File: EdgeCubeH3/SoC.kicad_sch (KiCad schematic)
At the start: 38 parts, among them Q4 NPN, SW1 RST, U1 H3, Y1 24M, Y2 32K

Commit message: Schematic update, PCB started
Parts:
- added R42: 10M, Resistor_SMD:R_0603_1608Metric, symbol Device:R
- added SW2: PWR, Button_Switch_SMD:Button_6x3mm, symbol Switch:SW_Push
- SW1: footprint (none) -> Button_Switch_SMD:Button_6x3mm
- U1: footprint Lib:BGA347_H3_AWT-M -> cm0:FBGA-347_14x14mm_Layout21x21_P0.65mm
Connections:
- net GND: now also SW2.1
- net at R41.1, TP2.1, U1.R1 (PL3): now also SW2.2
- net at C26.2, U1.U4 (X32KOUT), Y2.3: now also R42.1
- net at C27.2, U1.V5 (X32KIN), Y2.1: now also R42.2
- net SPI0_CS: now reaches U1.B15 (PC3)
- net SPI0_CLK: now reaches U1.B16 (PC2)
- net SPI0_MOSI: now reaches U1.C15 (PC0)
- net SPI0_MISO: now reaches U1.C16 (PC1)
- no-connect marks 117 -> 113
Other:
- moved on the sheet: R33

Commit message: PCB design at ~90%
- re-arrangement of components
- connecting dram
- connecting ports
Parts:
- R36: footprint Resistor_SMD:R_0603_1608Metric_Pad0.98x0.95mm_HandSolder -> Resistor_SMD:R_0603_1608Metric
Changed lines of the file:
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@@
 			)
 		)
-		(property "Footprint" "Resistor_SMD:R_0603_1608Metric_Pad0.98x0.95mm_HandSolder"
+		(property "Footprint" "Resistor_SMD:R_0603_1608Metric"
 			(at 238.252 114.3 90)
 			(hide yes)

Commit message: PCB at 95%
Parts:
- removed SW1: RST, Button_Switch_SMD:Button_6x3mm, symbol Switch:SW_Push
- removed SW2: PWR, Button_Switch_SMD:Button_6x3mm, symbol Switch:SW_Push

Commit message: Compleating PCB design
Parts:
- added C45: 100n, Resistor_SMD:R_0402_1005Metric, symbol Device:C
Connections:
- net GND: now also C45.2
- net VREF: now also C45.1
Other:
- note added: "RESET Circuit"
- moved on the sheet: C29, C30, Q4, R37, R38, R39

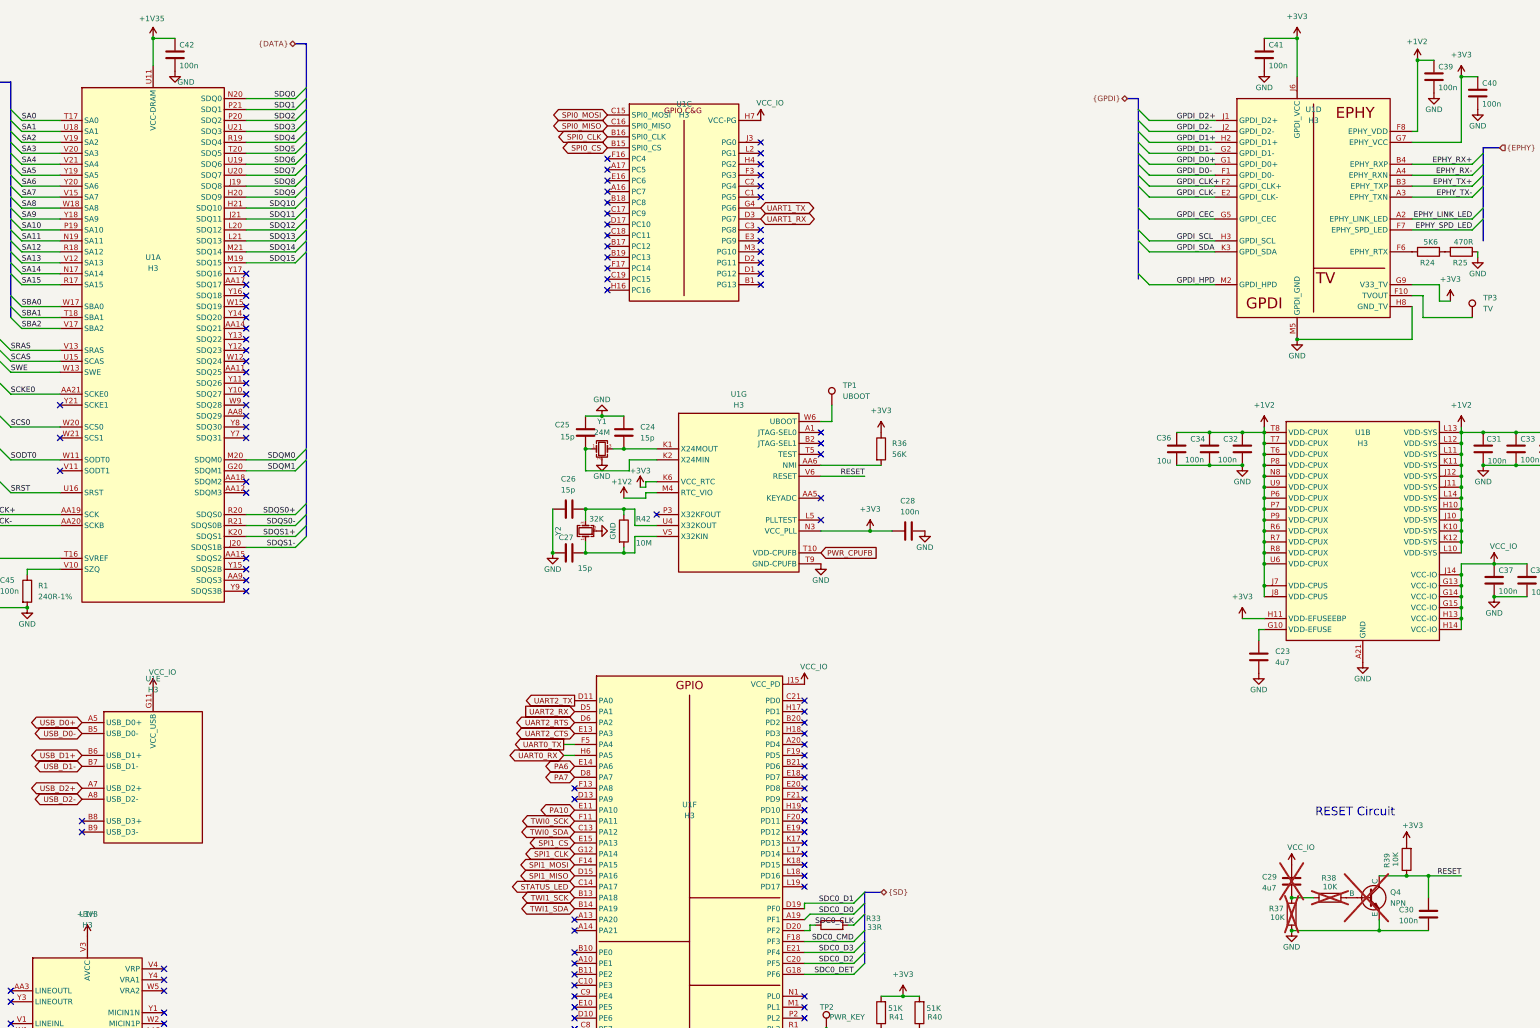
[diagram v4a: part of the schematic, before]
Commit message: Small changes to PCB, updated schematic and readme
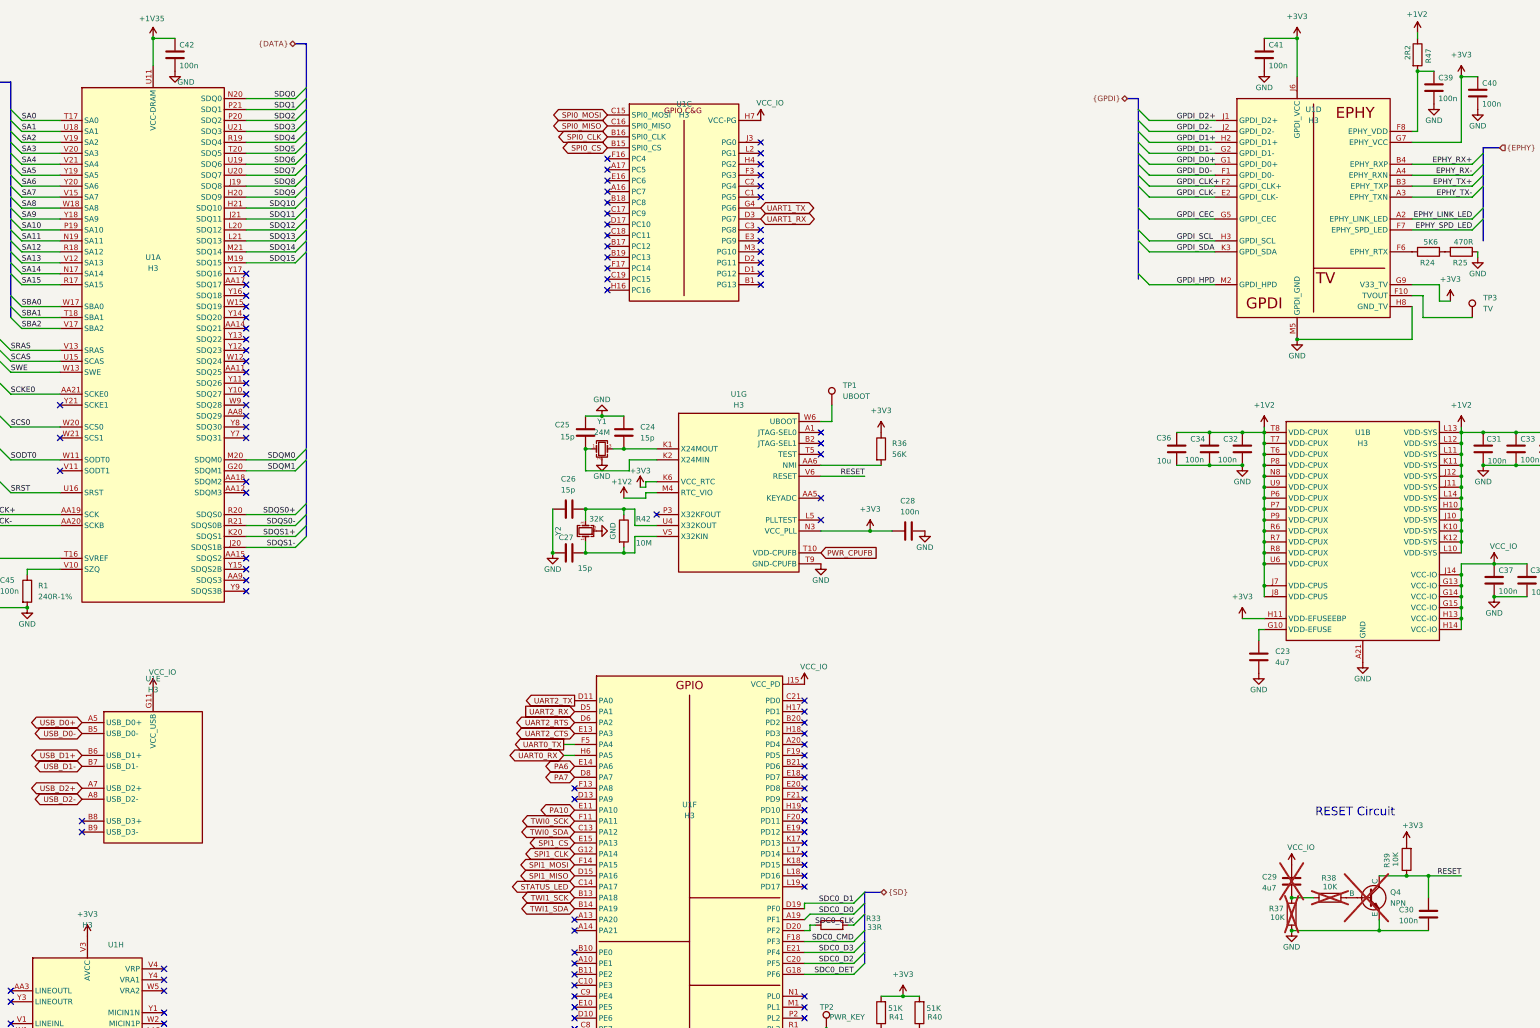
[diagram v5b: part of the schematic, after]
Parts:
- added R47: 2R2, Resistor_SMD:R_0603_1608Metric, symbol Device:R
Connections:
- net +1V2: now also R47.1; no longer C39.1, U1.F8 (EPHY_VDD)
- new net: C39.1, R47.2, U1.F8 (EPHY_VDD)
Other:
- moved on the sheet: C39
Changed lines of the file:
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@@
 	(title_block
 		(title "EdgeCubeH3")
-		(date "2026-05-07")
-		(rev "0.1")
+		(date "2026-05-21")
+		(rev "rev.A")
 		(company "github.com/sentoxo/EdgeCubeH3")
 	)
@@
 	)
 	(junction
-		(at 364.49 24.13)
-		(diameter 0)
-		(color 0 0 0 0)
-	)
-	(junction
 		(at 387.35 118.11)
 		(diameter 0)
@@
 	)
 	(junction
+		(at 364.49 26.67)
+		(diameter 0)
+		(color 0 0 0 0)
+	)
+	(junction
 		(at 379.73 110.49)
 		(diameter 0)
@@
 	(wire
 		(pts
+			(xy 364.49 26.67) (xy 364.49 40.64)
+		)
+		(stroke
+			(width 0)
+			(type default)
+		)
+	)
+	(wire
+		(pts
 			(xy 387.35 118.11) (xy 394.97 118.11)
 		)
@@
 	(wire
 		(pts
-			(xy 364.49 24.13) (xy 368.3 24.13)
+			(xy 364.49 26.67) (xy 368.3 26.67)
 		)
 		(stroke
@@
 	(wire
 		(pts
-			(xy 364.49 24.13) (xy 364.49 40.64)
-		)
-		(stroke
-			(width 0)
-			(type default)
-		)
-	)
-	(wire
-		(pts
 			(xy 40.64 53.34) (xy 49.53 53.34)
 		)
@@
 	(wire
 		(pts
+			(xy 364.49 17.78) (xy 364.49 19.05)
+		)
+		(stroke
+			(width 0)
+			(type default)
+		)
+	)
+	(wire
+		(pts
 			(xy 92.71 129.54) (xy 104.14 129.54)
 		)
@@
 	(symbol
 		(lib_id "power:GND")
-		(at 368.3 31.75 0)
+		(at 368.3 34.29 0)
 		(unit 1)
 		(body_style 1)
@@
 		(dnp no)
 		(property "Reference" "#PWR058"
-			(at 368.3 38.1 0)
+			(at 368.3 40.64 0)
 			(hide yes)
 			(show_name no)
@@
 		)
 		(property "Value" "GND"
-			(at 368.3 35.56 0)
+			(at 368.3 38.1 0)
 			(show_name no)
 			(do_not_autoplace no)
@@
 		)
 		(property "Footprint" ""
-			(at 368.3 31.75 0)
+			(at 368.3 34.29 0)
 			(hide yes)
 			(show_name no)
@@
 		)
 		(property "Datasheet" ""
-			(at 368.3 31.75 0)
+			(at 368.3 34.29 0)
 			(hide yes)
 			(show_name no)
@@
 		)
 		(property "Description" "Power symbol creates a global label with name \"GND\" , ground"
-			(at 368.3 31.75 0)
+			(at 368.3 34.29 0)
 			(hide yes)
 			(show_name no)
@@
 	(symbol
 		(lib_id "Device:C")
-		(at 368.3 27.94 0)
+		(at 368.3 30.48 0)
 		(unit 1)
 		(body_style 1)
@@
 		(dnp no)
 		(property "Reference" "C39"
-			(at 369.316 25.654 0)
+			(at 369.316 28.194 0)
 			(show_name no)
 			(do_not_autoplace no)
@@
 		)
 		(property "Value" "100n"
-			(at 369.316 30.48 0)
+			(at 369.316 33.02 0)
 			(show_name no)
 			(do_not_autoplace no)
@@
 		)
 		(property "Footprint" "Capacitor_SMD:C_0402_1005Metric"
-			(at 369.2652 31.75 0)
+			(at 369.2652 34.29 0)
 			(hide yes)
 			(show_name no)
@@
 		)
 		(property "Datasheet" ""
-			(at 368.3 27.94 0)
+			(at 368.3 30.48 0)
 			(hide yes)
 			(show_name no)
@@
 		)
 		(property "Description" "Unpolarized capacitor"
-			(at 368.3 27.94 0)
+			(at 368.3 30.48 0)
 			(hide yes)
 			(show_name no)
@@
 	(symbol
 		(lib_id "Device:R")
+		(at 364.49 22.86 0)
+		(unit 1)
+		(body_style 1)
+		(exclude_from_sim no)
+		(in_bom yes)
+		(on_board yes)
+		(in_pos_files yes)
+		(dnp no)
+		(property "Reference" "R47"
+			(at 367.03 23.114 90)
+			(show_name no)
+			(do_not_autoplace no)
+			(effects
+				(font
+					(size 1.27 1.27)
+				)
+			)
+		)
+		(property "Value" "2R2"
+			(at 362.204 22.352 90)
+			(show_name no)
+			(do_not_autoplace no)
+			(effects
+				(font
+					(size 1.27 1.27)
+				)
+			)
+		)
+		(property "Footprint" "Resistor_SMD:R_0603_1608Metric"
+			(at 362.712 22.86 90)
+			(hide yes)
+			(show_name no)
+			(do_not_autoplace no)
+			(effects
+				(font
+					(size 1.27 1.27)
+				)
+			)
+		)
+		(property "Datasheet" ""
+			(at 364.49 22.86 0)
+			(hide yes)
+			(show_name no)
+			(do_not_autoplace no)
+			(effects
+				(font
+					(size 1.27 1.27)
+				)
+			)
+		)
+		(property "Description" "Resistor"
+			(at 364.49 22.86 0)
+			(hide yes)
+			(show_name no)
+			(do_not_autoplace no)
+			(effects
+				(font
+					(size 1.27 1.27)
+				)
+			)
+		)
+		(pin "1"
+		)
+		(pin "2"
+		)
+		(instances
+			(project "EdgeCubeH3"
+				(path "/36b001b0-3d06-4fed-b406-d82b909f7864/342a6ee4-1ac6-4677-8762-5b9ce3280011"
+					(reference "R47")
+					(unit 1)
+				)
+			)
+		)
+	)
+	(symbol
+		(lib_id "Device:R")
 		(at 41.91 147.32 0)
 		(unit 1)
@@
 		(in_pos_files yes)
 		(dnp no)
-		(fields_autoplaced yes)
 		(property "Reference" "U1"
-			(at 55.88 222.25 0)
+			(at 62.484 229.362 0)
 			(show_name no)
 			(do_not_autoplace no)
@@
 	(symbol
 		(lib_id "power:+3V3")
-		(at 364.49 24.13 0)
+		(at 364.49 17.78 0)
 		(unit 1)
 		(body_style 1)
@@
 		(dnp no)
 		(property "Reference" "#PWR051"
-			(at 364.49 27.94 0)
+			(at 364.49 21.59 0)
 			(hide yes)
 			(show_name no)
@@
 		)
 		(property "Value" "+1V2"
-			(at 361.95 19.812 0)
+			(at 361.95 13.462 0)
 			(show_name no)
 			(do_not_autoplace no)
@@
 		)
 		(property "Footprint" ""
-			(at 364.49 24.13 0)
+			(at 364.49 17.78 0)
 			(hide yes)
 			(show_name no)
@@
 		)
 		(property "Datasheet" ""
-			(at 364.49 24.13 0)
+			(at 364.49 17.78 0)
 			(hide yes)
 			(show_name no)
@@
 		)
 		(property "Description" "Power symbol creates a global label with name \"+3V3\""
-			(at 364.49 24.13 0)
+			(at 364.49 17.78 0)
 			(hide yes)
 			(show_name no)
